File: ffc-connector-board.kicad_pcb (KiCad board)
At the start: 2 copper layers, 100 x 100 mm, 19 parts, among them J1 1-84953-0, J2 Conn_01x10_Male, J3 Conn_01x10_Male, J4 200485-0710, J5 200528-0100, J6 Conn_01x10_Male, J7 505110-1092, J8 Conn_01x10_Male

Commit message: Fix silkscreen
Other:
- board text removed: "J1"
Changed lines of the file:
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@@
     (effects (font (size 1.5 1.5) (thickness 0.3)) (justify mirror))
-  )
-  (gr_text "J1" (at 98.586428 87.955 -180) (layer "B.SilkS")
-    (effects (font (size 1.27 1.27) (thickness 0.254)) (justify mirror))
   )
   (gr_text "PMIC_VOUT_EN" (at 122 133) (layer "B.SilkS")

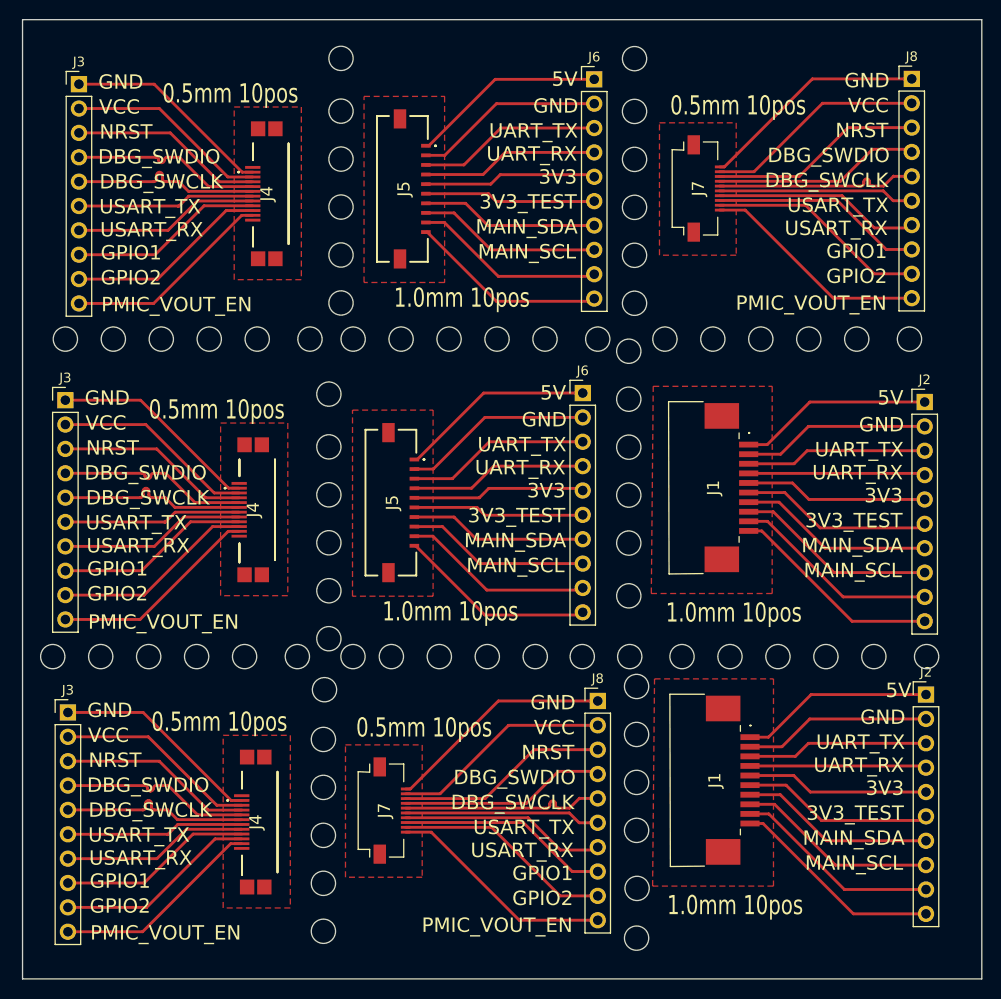
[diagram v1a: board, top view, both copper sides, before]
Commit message: 2nd version with smaller connectors
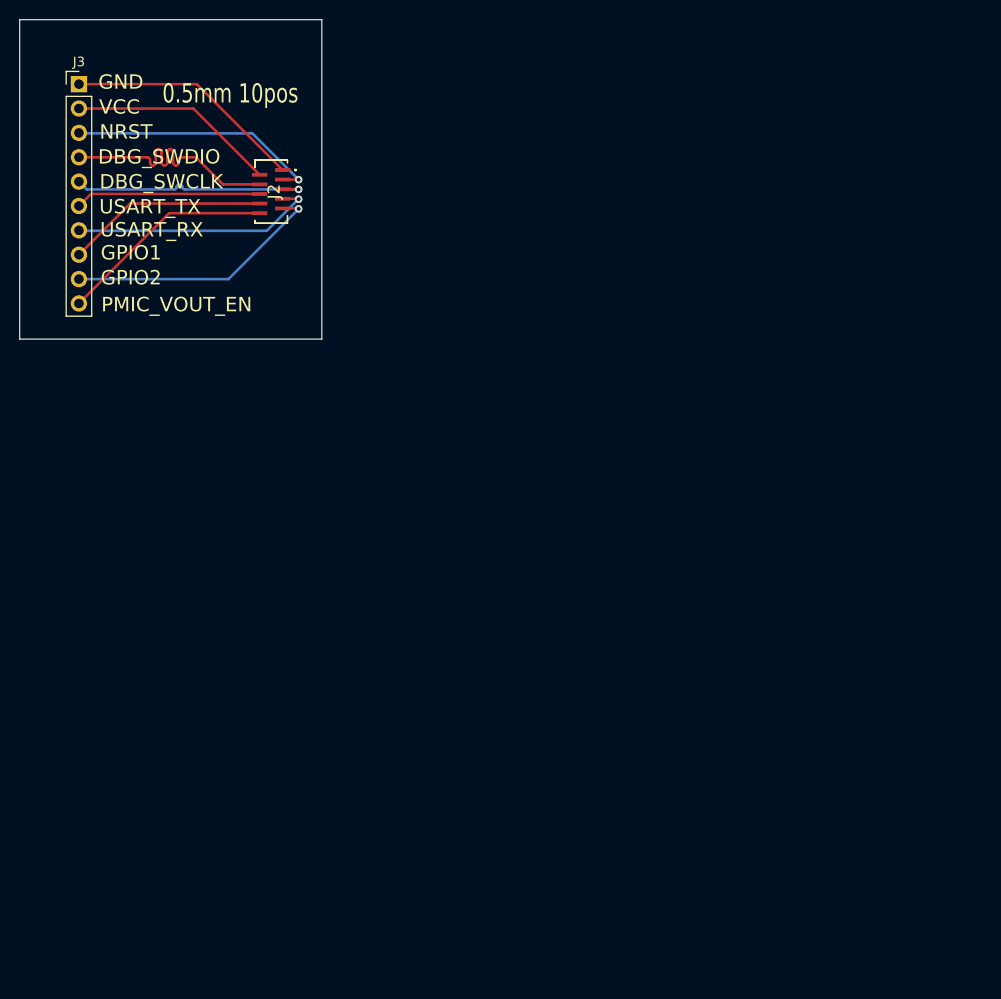
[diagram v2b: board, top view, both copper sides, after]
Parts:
- removed G***: LOGO, FOSS:OSHW
- removed J1 (x2): 1-84953-0, Library:1849530
- removed the J2 at (166.0, 109.6)
- removed the J2 at (165.8, 79.1)
- removed the J3 at (76.3, 78.9)
- removed the J3 at (76.5, 111.4)
- removed J4 (x3): 200485-0710, Library:2004850710
- removed J5 (x2): 200528-0100, Library:2005280100
- removed J6 (x2), J8 (x2): Conn_01x10_Male, Connector_PinHeader_2.54mm:PinHeader_1x10_P2.54mm_Vertical
- removed J7 (x2): 505110-1092, Library:5051101092
- added J2: 78119-1020, SamacSys_Parts:781191020, F.Cu at (97.7, 57.1)
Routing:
- net Net-(J7-Pad10): track 47.7 -> 0.00 mm
- net Net-(J7-Pad1): track 47.7 -> 0.00 mm
- net Net-(J7-Pad9): track 46.0 -> 0.00 mm
- net Net-(J7-Pad2): track 46.0 -> 0.00 mm
- net Net-(J1-Pad10): track 44.5 -> 0.00 mm
- net Net-(J7-Pad8): track 44.3 -> 0.00 mm
- net Net-(J7-Pad3): track 44.3 -> 0.00 mm
- net Net-(J1-Pad9): track 43.2 -> 0.00 mm
- net Net-(J7-Pad7): track 43.1 -> 0.00 mm
- net Net-(J7-Pad4): track 43.0 -> 0.00 mm
- net Net-(J3-Pin_10): track 65.8 -> 22.7 mm
- net Net-(J7-Pad5): track 42.8 -> 0.00 mm
- net Net-(J1-Pad8): track 42.0 -> 0.00 mm
- net Net-(J3-Pin_2): track 63.2 -> 21.7 mm
- net Net-(J5-Pad10): track 41.3 -> 0.00 mm
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- removed copper zone on F.Cu, net GND
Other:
- board size 100 x 100 mm -> 31.5 x 33.3 mm
- board text removed: "1.0mm 10pos"
- board text removed: "3V3"
- board text removed: "3V3_TEST"
- board text removed: "5V"
- board text removed: "Conn_01x10_Male"
- board text removed: "Designed with KiCad"
- board text removed: "MAIN_SCL"
- board text removed: "MAIN_SDA"
- board text removed: "UART_RX"
- board text removed: "UART_TX"
- board text removed: "Version 0.1"
- board text removed: "https://github.com/Sedictious/ffc-connector-board"
